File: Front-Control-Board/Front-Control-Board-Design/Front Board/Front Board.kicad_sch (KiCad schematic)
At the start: 25 parts, among them J1 Conn_01x08, J2 Conn_01x23, Q1 2N7002, U1 MAX33054EASA+T, U2 TS2940CP33 ROG, U3 ESP32-DevKitC

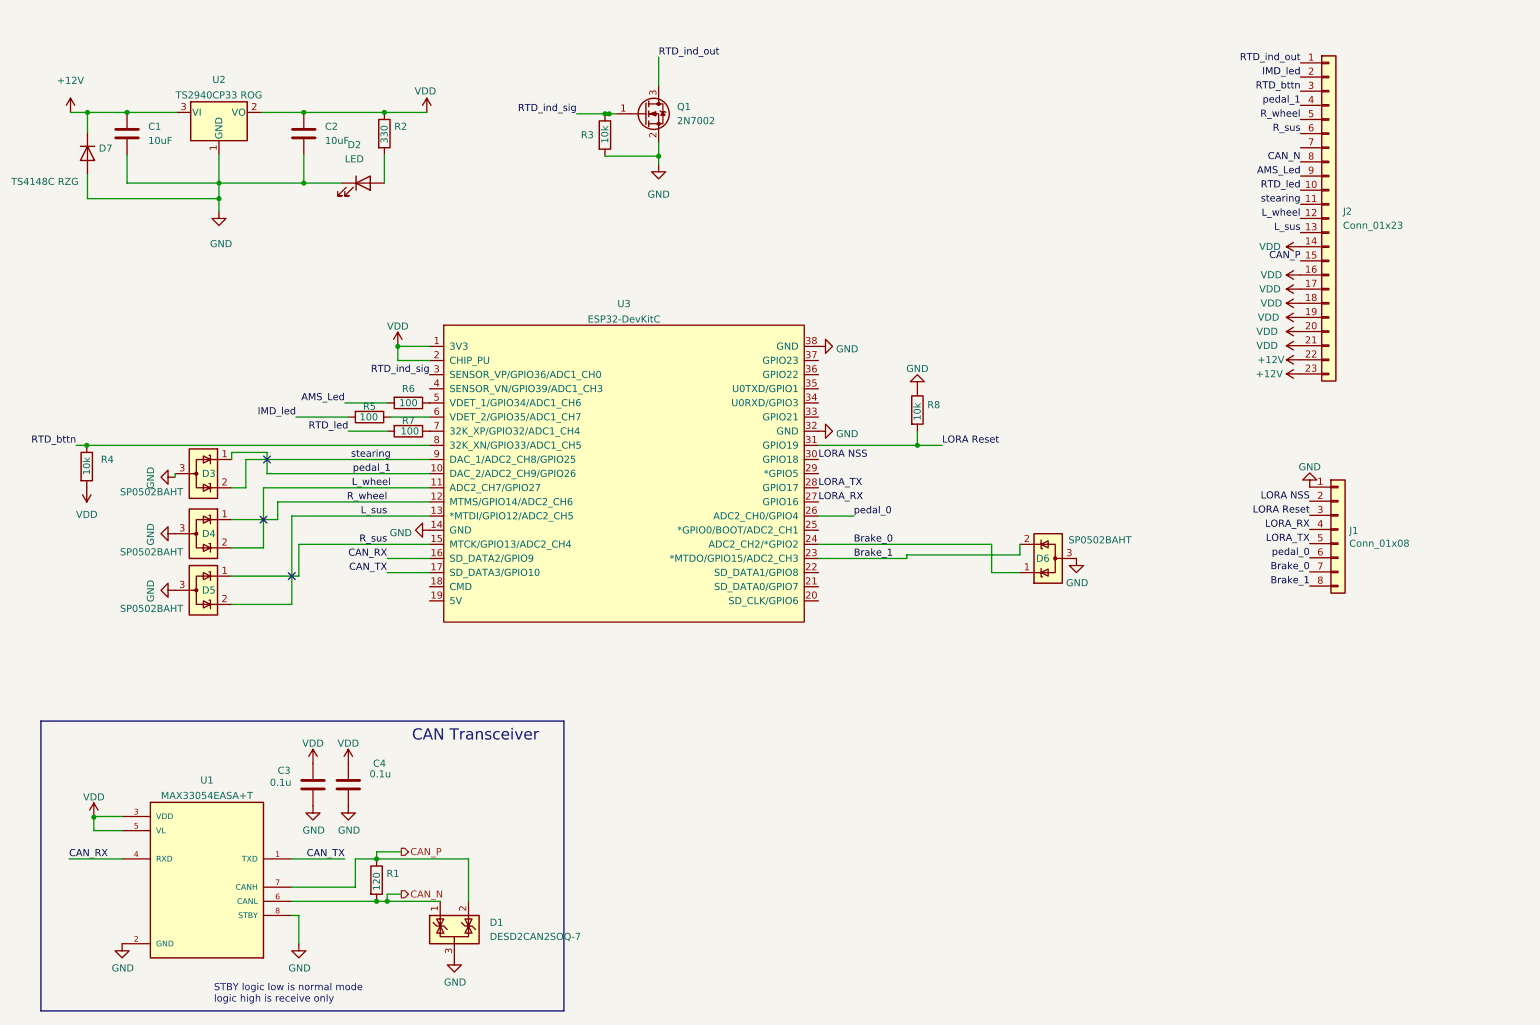
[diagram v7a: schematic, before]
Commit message: updated pins schematic
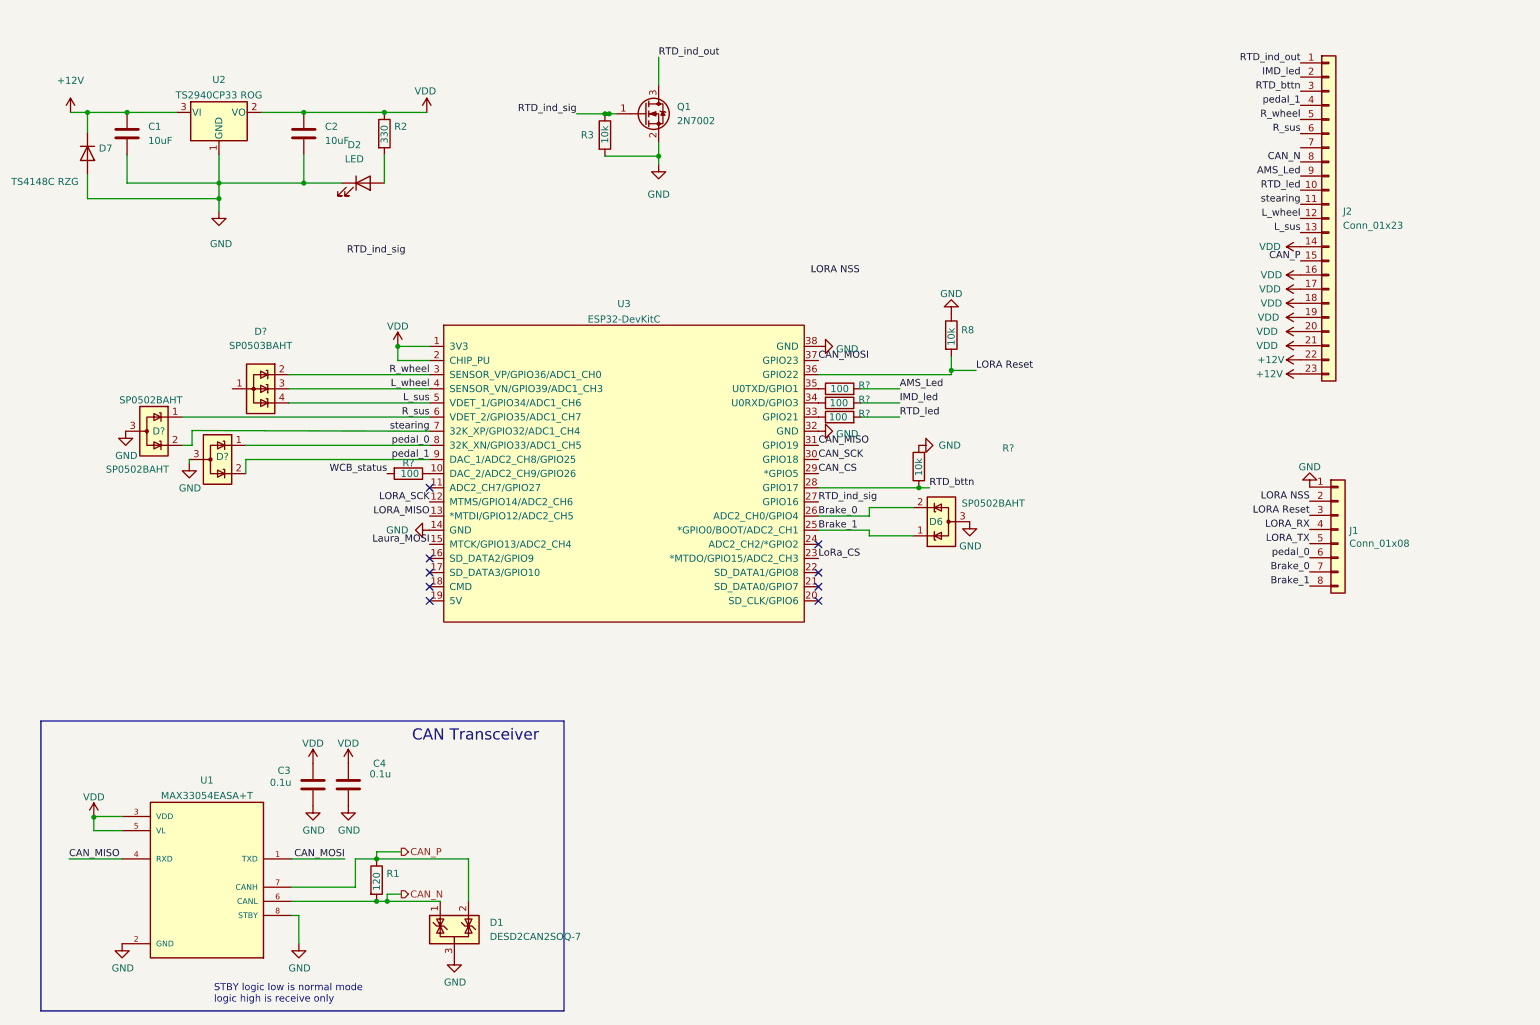
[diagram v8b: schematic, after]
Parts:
- removed D3, D4, D5: SP0502BAHT, Package_TO_SOT_SMD:SOT-23, symbol Power_Protection:SP0502BAHT
- removed R4: 10k, Resistor_SMD:R_0603_1608Metric_Pad0.98x0.95mm_HandSolder, symbol Device:R
- removed R5, R6, R7: 100, Resistor_SMD:R_0603_1608Metric_Pad0.98x0.95mm_HandSolder, symbol Device:R
- added D?: SP0503BAHT, Package_TO_SOT_SMD:SOT-143, symbol Power_Protection:SP0503BAHT
- added D? (x2): SP0502BAHT, Package_TO_SOT_SMD:SOT-23, symbol Power_Protection:SP0502BAHT
- added R? (x4): 100, Resistor_SMD:R_0603_1608Metric_Pad0.98x0.95mm_HandSolder, symbol Device:R
- added R?: 10k, Resistor_SMD:R_0603_1608Metric_Pad0.98x0.95mm_HandSolder, symbol Device:R
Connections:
- net AMS_Led: now also R?.2
- net Brake_0: now also D6.2 (K), U3.26 (ADC2_CH0/GPIO4); no longer D6.1 (K), U3.24 (ADC2_CH2/*GPIO2)
- net Brake_1: now also D6.1 (K), U3.25 (*GPIO0/BOOT/ADC2_CH1); no longer D6.2 (K), U3.23 (*MTDO/GPIO15/ADC2_CH3)
- net GND: now also D?.3 (A), D?.3 (A), R?.2
- net IMD_led: now also R?.1
- net LORA NSS: no longer U3.30 (GPIO18)
- net LORA Reset: now also U3.36 (GPIO22); no longer U3.31 (GPIO19)
- net LORA_RX: no longer U3.27 (GPIO16)
- net LORA_TX: no longer U3.28 (GPIO17)
- net L_sus: now also U3.5 (VDET_1/GPIO34/ADC1_CH6), D?.4 (K); no longer U3.13 (*MTDI/GPIO12/ADC2_CH5)
- net L_wheel: now also U3.4 (SENSOR_VN/GPIO39/ADC1_CH3), D?.3 (K); no longer U3.11 (ADC2_CH7/GPIO27)
- net RTD_bttn: now also U3.28 (GPIO17), R?.1; no longer U3.8 (32K_XN/GPIO33/ADC1_CH5)
- net RTD_ind_sig: now also U3.27 (GPIO16); no longer U3.3 (SENSOR_VP/GPIO36/ADC1_CH0)
- net RTD_led: now also R?.2
- net R_sus: now also U3.6 (VDET_2/GPIO35/ADC1_CH7), D?.1 (K); no longer U3.15 (MTCK/GPIO13/ADC2_CH4)
- net R_wheel: now also U3.3 (SENSOR_VP/GPIO36/ADC1_CH0), D?.2 (K); no longer U3.12 (MTMS/GPIO14/ADC2_CH6)
- net pedal_0: now also U3.8 (32K_XN/GPIO33/ADC1_CH5), D?.1 (K); no longer U3.26 (ADC2_CH0/GPIO4)
- net pedal_1: now also U3.9 (DAC_1/ADC2_CH8/GPIO25), D?.2 (K); no longer U3.10 (DAC_2/ADC2_CH9/GPIO26)
- net stearing: now also U3.7 (32K_XP/GPIO32/ADC1_CH4), D?.2 (K); no longer U3.9 (DAC_1/ADC2_CH8/GPIO25)
- net CAN_CS: now reaches U3.29 (*GPIO5)
- net at U3.33 (GPIO21): now also R?.1
- net at U3.34 (U0RXD/GPIO3): now also R?.2
- net at U3.35 (U0TXD/GPIO1): now also R?.1
- net CAN_MOSI: now reaches U3.37 (GPIO23)
- net CAN_MOSI: now also U1.1 (TXD)
- net CAN_RX: no longer names the net of U3.16 (SD_DATA2/GPIO9)
- net CAN_RX: no longer U1.4 (RXD)
- net CAN_TX: no longer names the net of U3.17 (SD_DATA3/GPIO10)
- net CAN_TX: no longer U1.1 (TXD)
- new net: R?.1, U3.10 (DAC_2/ADC2_CH9/GPIO26)
- new net CAN_MISO: U1.4 (RXD), U3.31 (GPIO19)
- new net CAN_SCK: U3.30 (GPIO18)
- new net LORA_MISO: U3.13 (*MTDI/GPIO12/ADC2_CH5)
- new net LORA_SCK: U3.12 (MTMS/GPIO14/ADC2_CH6)
- new net Laura_MOSI: U3.15 (MTCK/GPIO13/ADC2_CH4)
- new net LoRa_CS: U3.23 (*MTDO/GPIO15/ADC2_CH3)
- new net WCB_status: R?.2
- no-connect marks 3 -> 9
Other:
- moved on the sheet: D6, R8
